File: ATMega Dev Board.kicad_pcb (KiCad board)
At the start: 4 copper layers, 84 x 38.1 mm, 44 parts, among them J1 Conn_01x09, J2 Conn_01x04, J3 Conn_01x09, J4 SPI header, J5 USB-C_31-M-12, Q1 S8050, Q2 2N7002, Q3 HL6042, Q4 HL6042, SW1 SW_SPST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

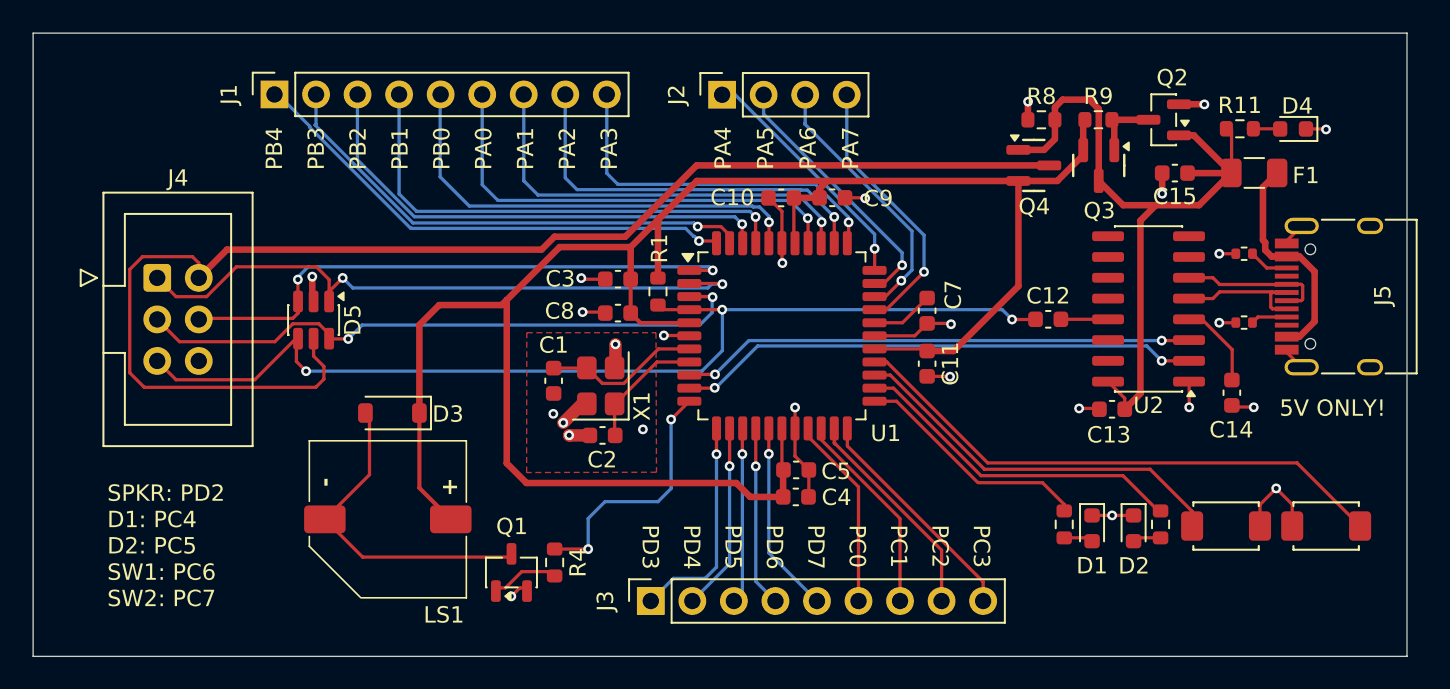
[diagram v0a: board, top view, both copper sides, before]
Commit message: corrected usb connections
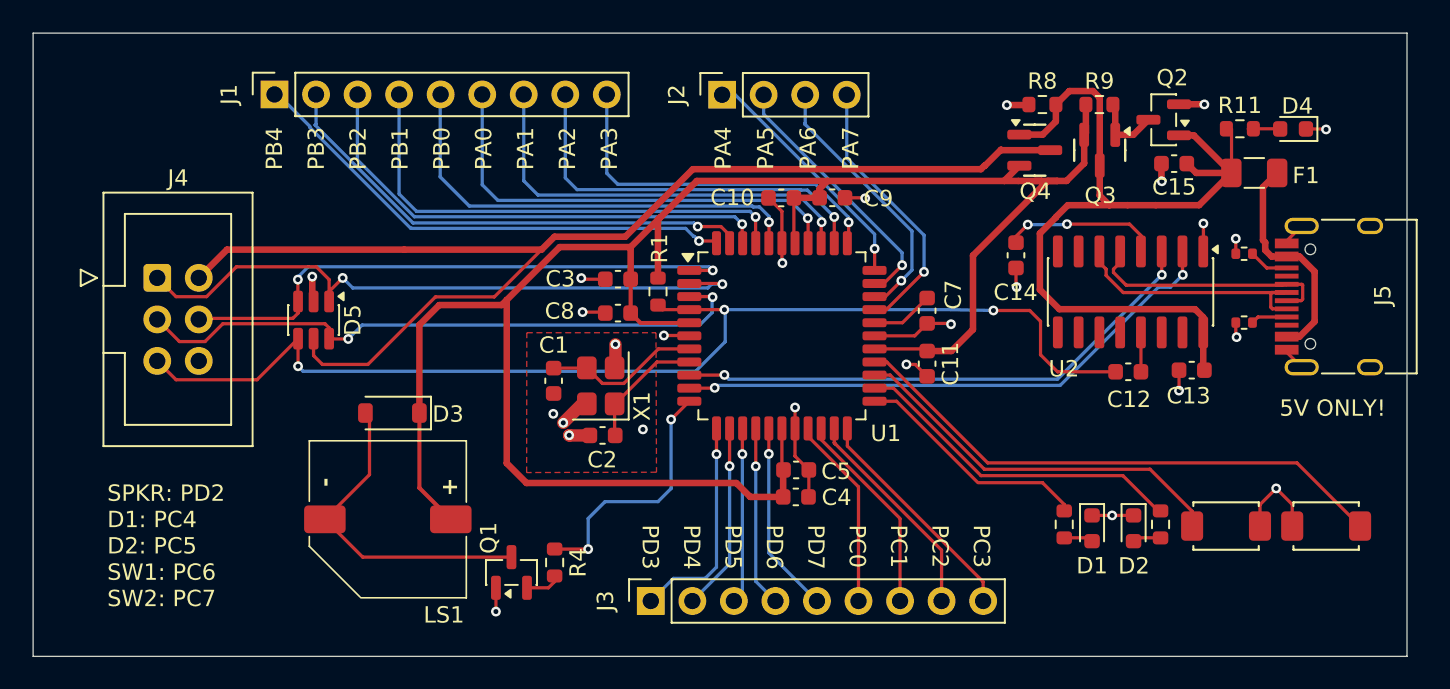
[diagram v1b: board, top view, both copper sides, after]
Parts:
- Q1: footprint Package_TO_SOT_SMD:SOT-23-3 -> Package_TO_SOT_SMD:SOT-23
- moved C14 15.6 mm to (138.2, 86.2)
- moved C12 5.85 mm to (145.0, 93.3)
- moved C13 5.42 mm to (148.9, 93.2)
- moved U2 1.51 mm to (145.2, 88.5), turned to -90 degrees
- moved Q3 0.93 mm to (143.3, 79.8)
- moved Q4 0.93 mm to (139.3, 79.8)
- moved R9 0.93 mm to (143.2, 77.0)
- moved R8 0.93 mm to (139.8, 77.0)
- moved C15 0.58 mm to (147.8, 80.6)
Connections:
- J5 pad A6: /UD- -> /UD+
- J5 pad A7: /UD+ -> /UD-
- J5 pad B6: /UD- -> /UD+
- J5 pad B7: /UD+ -> /UD-
- Q1 pad 1: Net-(Q1-B) -> GND
- Q1 pad 2: GND -> Net-(Q1-B)
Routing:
- net VSPI: track 82.0 -> 73.4 mm
- net VBUS: track 45.7 -> 53.3 mm
- net /RST: track 64.3 -> 71.6 mm
- net /UD-: track 9.00 -> 16.0 mm
- net /UD+: track 9.02 -> 15.3 mm
- net VCC: track 126.1 -> 130.3 mm
- net Net-(U2-V3): track 5.37 -> 9.62 mm, vias 0 -> 2
- net /URXD: track 32.0 -> 34.5 mm
- net Net-(Q1-B): track 4.11 -> 2.19 mm
- net /UTXD: track 31.4 -> 33.1 mm

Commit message: added USB ESD protection
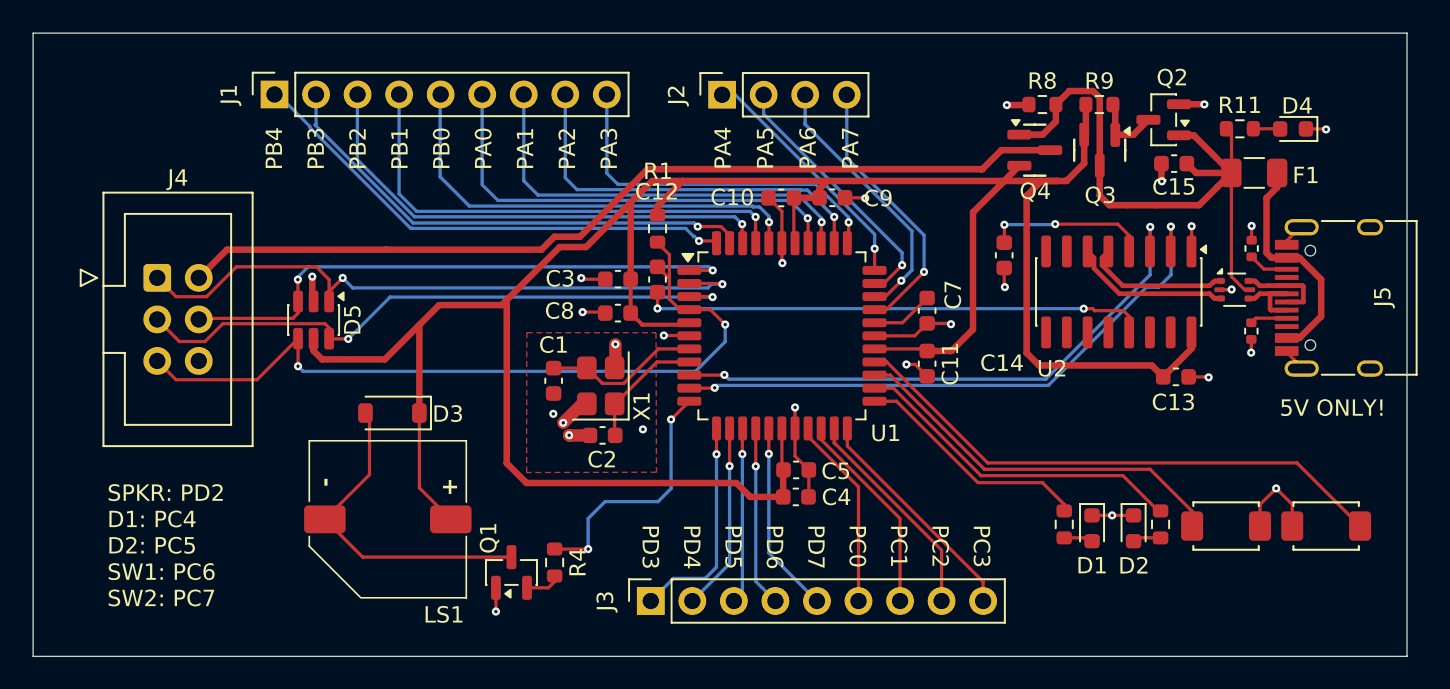
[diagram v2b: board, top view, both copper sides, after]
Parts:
- added U3: USBLC6-2P6, Package_TO_SOT_SMD:SOT-666, F.Cu at (151.5, 88.3)
- moved C12 29.3 mm to (116.2, 87.7), turned to -90 degrees
- moved R1 3.85 mm to (116.2, 84.6)
- moved C13 1.05 mm to (147.9, 93.7), turned to 180 degrees
- moved C14 0.72 mm to (137.4, 86.2)
- moved U2 0.72 mm to (144.4, 88.5)
- moved R5 0.68 mm to (152.5, 90.9), turned to 90 degrees
- moved R6 0.56 mm to (152.6, 85.8), turned to -90 degrees
- moved J5 0.08 mm to (158.8, 88.8)
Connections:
- C13 pad 2: VBUS -> VCC
- D5 pad 5: VSPI -> VCC
- J5 pad A6: /UD+ -> /UD_P
- J5 pad A7: /UD- -> /UD_N
- J5 pad B6: /UD+ -> /UD_P
- J5 pad B7: /UD- -> /UD_N
- U2 pad 16: VBUS -> VCC
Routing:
- net VCC: track 130.3 -> 162.2 mm
- net Net-(U2-~{DTR}): track 2.41 -> 31.2 mm, vias 0 -> 2
- net /RST: track 71.6 -> 48.7 mm, vias 3 -> 2
- net VSPI: track 73.4 -> 55.3 mm
- net VBUS: track 53.3 -> 38.8 mm
- net /UD+: track 15.3 -> 8.90 mm
- net /UD-: track 16.0 -> 9.72 mm
- net /UD_P: track 0.00 -> 5.45 mm
- net /UD_N: track 0.00 -> 5.43 mm
- net /URXD: track 34.5 -> 36.8 mm
- net /UTXD: track 33.1 -> 35.4 mm
- net /SCK: track 38.8 -> 38.3 mm
- net GND: track 52.5 -> 52.9 mm, vias 26 -> 27

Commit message: correct UART signalling
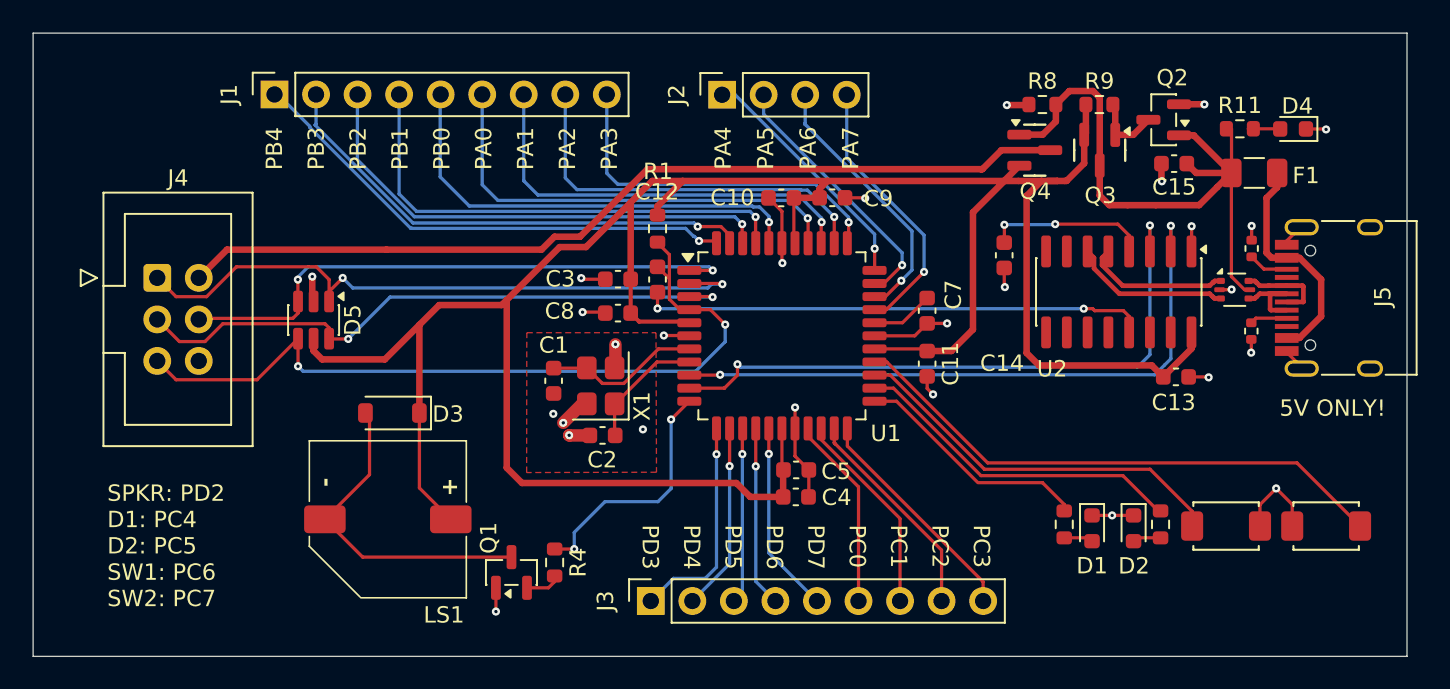
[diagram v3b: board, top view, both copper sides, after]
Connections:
- U2 pad 2: /URXD -> /UTXD
- U2 pad 3: /UTXD -> /URXD
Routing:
- net /UTXD: track 35.4 -> 39.6 mm
- net /URXD: track 36.8 -> 39.0 mm
- net GND: track 52.9 -> 52.3 mm
